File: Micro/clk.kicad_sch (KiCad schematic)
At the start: 8 parts, among them U52 Si5351A-B-GT, X2 ASV-2.5MHz, Y2 ABM8G-25.000MHZ-4Y-T3

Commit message: weird. idk why it made me change it
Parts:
- U53: value ~ -> TXU0304
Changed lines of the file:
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@@
   )
   (symbol (lib_id "New_Library:TXU0304") (at 83.82 69.85 90) (unit 1)
-    (in_bom yes) (on_board yes) (dnp no) (fields_autoplaced)
+    (in_bom yes) (on_board yes) (dnp no)
     (property "Reference" "U53" (at 93.98 69.85 90)
       (effects (font (size 1.27 1.27)) (justify right))
     )
-    (property "Value" "~" (at 81.915 68.58 0)
+    (property "Value" "TXU0304" (at 73.66 69.85 0)
       (effects (font (size 1.27 1.27)))
     )

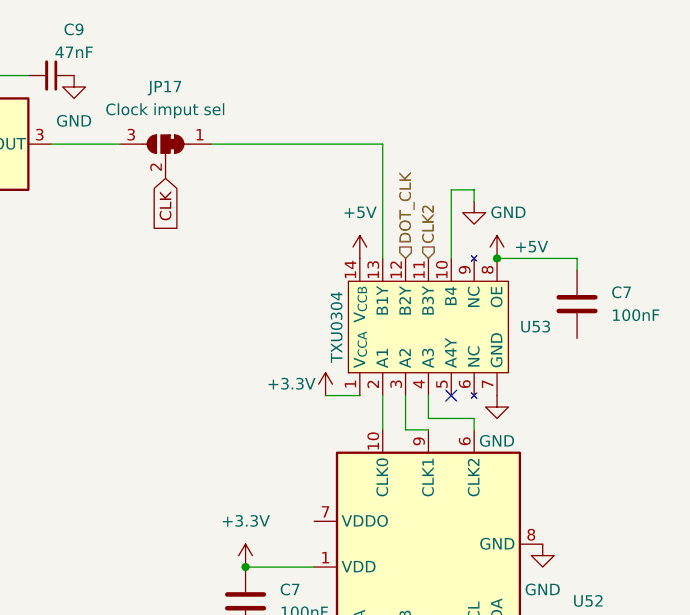
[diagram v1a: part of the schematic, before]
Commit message: Hardware: fixed error in schematic with clock moved dotclock to out 2 (better for jitter) allowed the replacement of 82c54 CPU CLK with CLK 2 moved nmi switch to a more reasonable location
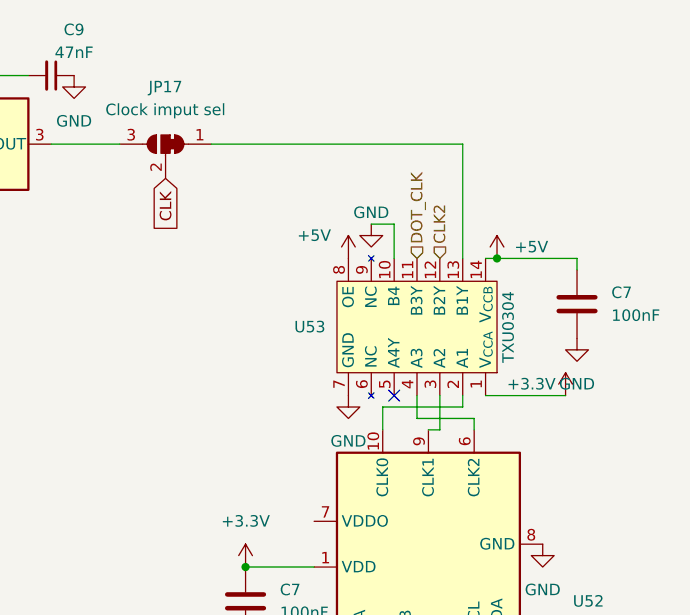
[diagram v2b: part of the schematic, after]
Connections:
- net CLK2: now also U53.12 (B2Y); no longer U53.11 (B3Y)
- net DOT_CLK: now also U53.11 (B3Y); no longer U53.12 (B2Y)
- net GND: now also C7.1
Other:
- moved on the sheet: U53
